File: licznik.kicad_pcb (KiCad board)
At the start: 2 copper layers, 71.1 x 43.2 mm, 23 parts, among them J1 Display, J2 Micro_SD_Card_Det, J3 Serial CS1, J4 Serial CS2, SW1 Wheel, SW2 Crank, SW3 Backlight, SW4 Right, SW5 Select, SW6 Left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

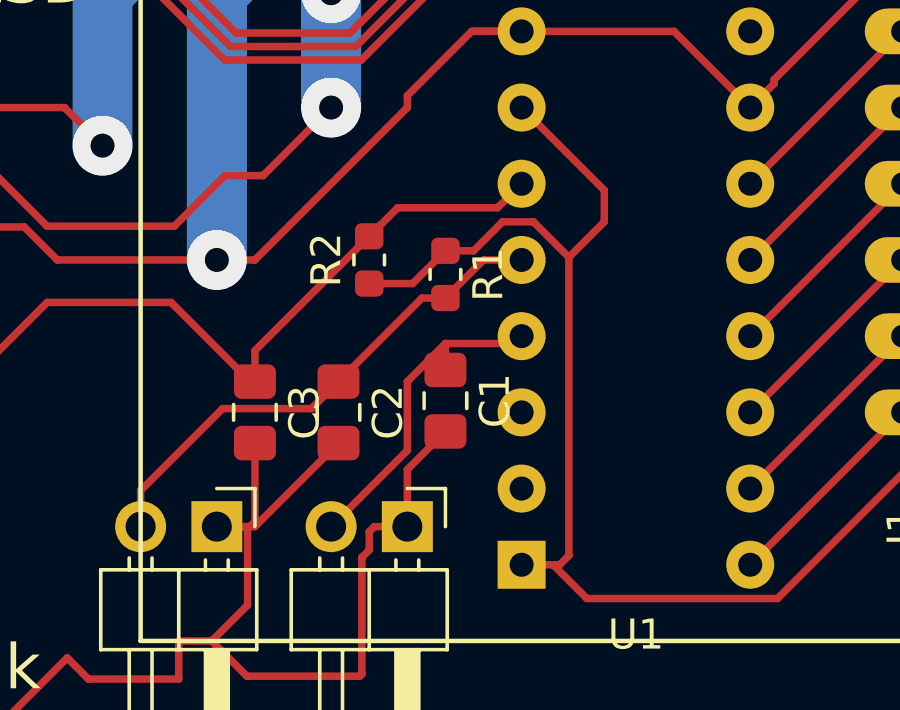
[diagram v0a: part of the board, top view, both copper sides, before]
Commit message: Add crank pull up resistor
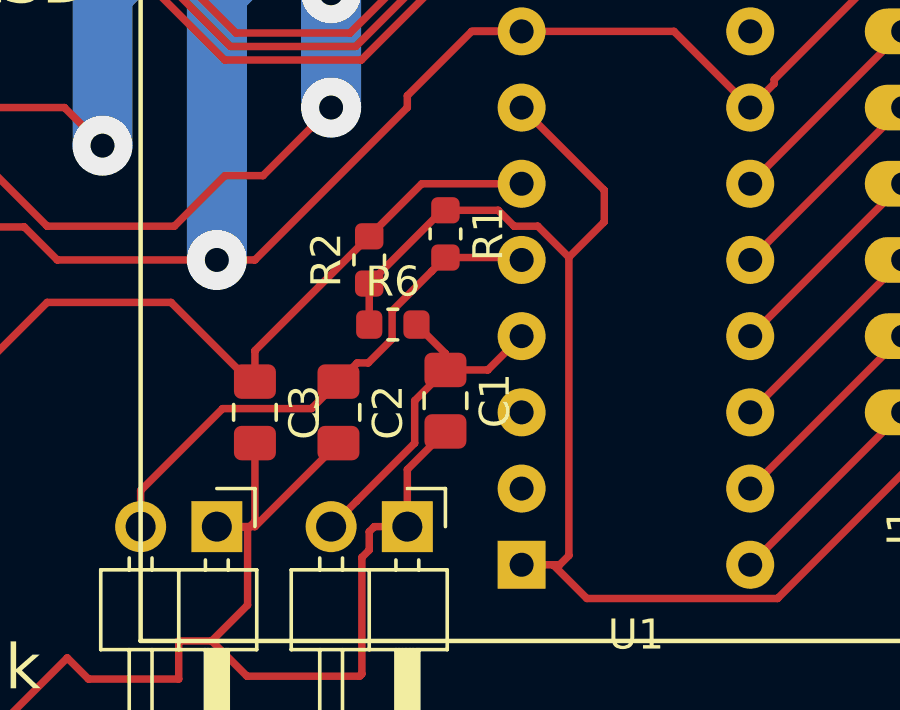
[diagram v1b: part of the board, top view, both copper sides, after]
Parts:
- added R6: 1K, Resistor_SMD:R_0603_1608Metric, F.Cu at (71.9, 184.2)
- moved R1 1.35 mm to (73.7, 181.1)
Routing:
- net +BATT: track 137.6 -> 139.3 mm
- net Net-(C2-Pad1): track 17.1 -> 17.7 mm
- net Net-(C1-Pad1): track 11.2 -> 11.7 mm
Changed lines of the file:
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@@
     (thickness 1.6)
     (drawings 14)
-    (tracks 267)
+    (tracks 273)
     (zones 0)
-    (modules 23)
+    (modules 24)
     (nets 26)
   )
@@
     (uvia_dia 0.3)
     (uvia_drill 0.1)
+  )
+  (module Resistor_SMD:R_0603_1608Metric (layer F.Cu)
+    (at 71.9075 184.15)
+    (descr "Resistor SMD 0603 (1608 Metric), square (rectangular) end terminal, IPC_7351 nominal, (Body size source: http://www.tortai-tech.com/upload/download/2011102023233369053.pdf), generated with kicad-footprint-generator")
+    (tags resistor)
+    (attr smd)
+    (fp_text reference R6 (at 0 -1.43) (layer F.SilkS)
+      (effects (font (size 1 1) (thickness 0.15)))
+    )
+    (fp_text value 1K (at 0 1.43) (layer F.Fab)
+      (effects (font (size 1 1) (thickness 0.15)))
+    )
+    (fp_line (start -0.8 0.4) (end -0.8 -0.4) (layer F.Fab) (width 0.1))
+    (fp_line (start -0.8 -0.4) (end 0.8 -0.4) (layer F.Fab) (width 0.1))
+    (fp_line (start 0.8 -0.4) (end 0.8 0.4) (layer F.Fab) (width 0.1))
+    (fp_line (start 0.8 0.4) (end -0.8 0.4) (layer F.Fab) (width 0.1))
+    (fp_line (start -0.162779 -0.51) (end 0.162779 -0.51) (layer F.SilkS) (width 0.12))
+    (fp_line (start -0.162779 0.51) (end 0.162779 0.51) (layer F.SilkS) (width 0.12))
+    (fp_line (start -1.48 0.73) (end -1.48 -0.73) (layer F.CrtYd) (width 0.05))
+    (fp_line (start -1.48 -0.73) (end 1.48 -0.73) (layer F.CrtYd) (width 0.05))
+    (fp_line (start 1.48 -0.73) (end 1.48 0.73) (layer F.CrtYd) (width 0.05))
+    (fp_line (start 1.48 0.73) (end -1.48 0.73) (layer F.CrtYd) (width 0.05))
+    (fp_text user %R (at 0 0) (layer F.Fab)
+      (effects (font (size 0.4 0.4) (thickness 0.06)))
+    )
+    (pad 1 smd roundrect (at -0.7875 0) (size 0.875 0.95) (layers F.Cu F.Paste F.Mask) (roundrect_rratio 0.25)
+      (net 22 +BATT))
+    (pad 2 smd roundrect (at 0.7875 0) (size 0.875 0.95) (layers F.Cu F.Paste F.Mask) (roundrect_rratio 0.25)
+      (net 1 "Net-(C1-Pad1)"))
+    (model ${KISYS3DMOD}/Resistor_SMD.3dshapes/R_0603_1608Metric.wrl
+      (at (xyz 0 0 0))
+      (scale (xyz 1 1 1))
+      (rotate (xyz 0 0 0))
+    )
   )
   (module Licznik:SD_pins (layer F.Cu)
@@
   )
   (module Resistor_SMD:R_0603_1608Metric (layer F.Cu)
-    (at 73.66 182.478122 270)
+    (at 73.66 181.1275 270)
     (descr "Resistor SMD 0603 (1608 Metric), square (rectangular) end terminal, IPC_7351 nominal, (Body size source: http://www.tortai-tech.com/upload/download/2011102023233369053.pdf), generated with kicad-footprint-generator")
     (tags resistor)
@@
   (gr_line (start 25.4 199.775622) (end 25.4 156.595622) (angle 90) (layer Edge.Cuts) (width 0.1))
   (gr_line (start 25.4 199.775622) (end 96.52 199.775622) (angle 90) (layer Edge.Cuts) (width 0.1))
-  (segment (start 75.955 184.780622) (end 76.2 184.535622) (width 0.25) (layer F.Cu) (net 1) (status 30))
-  (segment (start 73.66 184.780622) (end 75.955 184.780622) (width 0.25) (layer F.Cu) (net 1) (status 20))
-  (segment (start 73.66 185.662032) (end 73.66 184.780622) (width 0.25) (layer F.Cu) (net 1) (status 10))
-  (segment (start 73.66 184.780622) (end 72.39 186.050622) (width 0.25) (layer F.Cu) (net 1))
-  (segment (start 72.39 188.345622) (end 69.85 190.885622) (width 0.25) (layer F.Cu) (net 1) (status 20))
-  (segment (start 72.39 186.050622) (end 72.39 188.345622) (width 0.25) (layer F.Cu) (net 1))
+  (segment (start 75.07359 185.662032) (end 76.2 184.535622) (width 0.25) (layer F.Cu) (net 1))
+  (segment (start 73.66 185.662032) (end 75.07359 185.662032) (width 0.25) (layer F.Cu) (net 1))
+  (segment (start 70.699999 190.035623) (end 69.85 190.885622) (width 0.25) (layer F.Cu) (net 1))
+  (segment (start 72.63499 188.100632) (end 70.699999 190.035623) (width 0.25) (layer F.Cu) (net 1))
+  (segment (start 72.63499 186.687042) (end 72.63499 188.100632) (width 0.25) (layer F.Cu) (net 1))
+  (segment (start 73.66 185.662032) (end 72.63499 186.687042) (width 0.25) (layer F.Cu) (net 1))
+  (segment (start 73.66 185.115) (end 72.695 184.15) (width 0.25) (layer F.Cu) (net 1))
+  (segment (start 73.66 185.662032) (end 73.66 185.115) (width 0.25) (layer F.Cu) (net 1))
   (segment (start 83.82 179.455622) (end 88.9 174.375622) (width 0.25) (layer F.Cu) (net 5) (status 30))
   (segment (start 83.82 181.995622) (end 88.9 176.915622) (width 0.25) (layer F.Cu) (net 6) (status 30))
@@
   (segment (start 64.51499 183.410612) (end 67.31 186.205622) (width 0.25) (layer F.Cu) (net 14) (status 20))
   (segment (start 67.31 185.018122) (end 67.31 186.050622) (width 0.25) (layer F.Cu) (net 14) (status 20))
-  (segment (start 75.400001 180.255621) (end 72.072501 180.255621) (width 0.25) (layer F.Cu) (net 14) (status 10))
-  (segment (start 72.072501 180.255621) (end 71.12 181.208122) (width 0.25) (layer F.Cu) (net 14) (status 20))
-  (segment (start 76.2 179.455622) (end 75.400001 180.255621) (width 0.25) (layer F.Cu) (net 14) (status 30))
   (segment (start 71.12 181.208122) (end 67.31 185.018122) (width 0.25) (layer F.Cu) (net 14) (status 10))
   (segment (start 54.178976 189.615622) (end 60.383986 183.410612) (width 0.25) (layer F.Cu) (net 14))
   (segment (start 40.06 196.115622) (end 40.06 189.615622) (width 0.25) (layer F.Cu) (net 14) (status 30))
   (segment (start 40.06 189.615622) (end 54.178976 189.615622) (width 0.25) (layer F.Cu) (net 14) (status 10))
+  (segment (start 72.8725 179.455622) (end 76.2 179.455622) (width 0.25) (layer F.Cu) (net 14))
+  (segment (start 71.12 181.208122) (end 72.8725 179.455622) (width 0.25) (layer F.Cu) (net 14))
   (segment (start 63.5 189.683541) (end 63.5 190.885622) (width 0.25) (layer F.Cu) (net 15) (status 20))
   (segment (start 66.232909 186.950632) (end 63.5 189.683541) (width 0.25) (layer F.Cu) (net 15))
   (segment (start 69.19499 186.950632) (end 66.232909 186.950632) (width 0.25) (layer F.Cu) (net 15))
   (segment (start 70.095 186.050622) (end 69.19499 186.950632) (width 0.25) (layer F.Cu) (net 15) (status 10))
-  (segment (start 76.2 181.995622) (end 74.93 181.995622) (width 0.25) (layer F.Cu) (net 15) (status 10))
-  (segment (start 74.93 181.995622) (end 73.66 183.265622) (width 0.25) (layer F.Cu) (net 15) (status 20))
-  (segment (start 73.66 183.265622) (end 72.88 183.265622) (width 0.25) (layer F.Cu) (net 15) (status 10))
-  (segment (start 72.88 183.265622) (end 70.095 186.050622) (width 0.25) (layer F.Cu) (net 15) (status 20))
+  (segment (start 73.198388 182.376612) (end 73.66 181.915) (width 0.25) (layer F.Cu) (net 15))
+  (segment (start 71.88251 183.69249) (end 73.198388 182.376612) (width 0.25) (layer F.Cu) (net 15))
+  (segment (start 71.086744 185.42725) (end 71.88251 184.631484) (width 0.25) (layer F.Cu) (net 15))
+  (segment (start 71.88251 184.631484) (end 71.88251 183.69249) (width 0.25) (layer F.Cu) (net 15))
+  (segment (start 70.718372 185.42725) (end 71.086744 185.42725) (width 0.25) (layer F.Cu) (net 15))
+  (segment (start 70.095 186.050622) (end 70.718372 185.42725) (width 0.25) (layer F.Cu) (net 15))
+  (segment (start 76.119378 181.915) (end 76.2 181.995622) (width 0.25) (layer F.Cu) (net 15))
+  (segment (start 73.66 181.915) (end 76.119378 181.915) (width 0.25) (layer F.Cu) (net 15))
   (segment (start 66.889999 165.905623) (end 66.04 166.755622) (width 0.25) (layer F.Cu) (net 16) (status 30))
   (segment (start 70.33001 162.465612) (end 66.889999 165.905623) (width 0.25) (layer F.Cu) (net 16) (status 20))
@@
   (segment (start 73.66 165.968122) (end 74.1425 165.485622) (width 0.25) (layer F.Cu) (net 22))
   (segment (start 73.66 166.755622) (end 73.66 165.968122) (width 0.25) (layer F.Cu) (net 22) (status 10))
-  (segment (start 76.595002 180.725622) (end 77.77501 181.90563) (width 0.25) (layer F.Cu) (net 22))
-  (segment (start 75.56359 180.725622) (end 76.595002 180.725622) (width 0.25) (layer F.Cu) (net 22))
-  (segment (start 74.59859 181.690622) (end 75.56359 180.725622) (width 0.25) (layer F.Cu) (net 22))
-  (segment (start 73.66 181.690622) (end 74.59859 181.690622) (width 0.25) (layer F.Cu) (net 22) (status 10))
-  (segment (start 73.66 181.690622) (end 72.5675 182.783122) (width 0.25) (layer F.Cu) (net 22) (status 10))
-  (segment (start 72.5675 182.783122) (end 71.12 182.783122) (width 0.25) (layer F.Cu) (net 22) (status 20))
   (segment (start 81.759996 164.610624) (end 83.424998 162.945622) (width 0.25) (layer F.Cu) (net 22))
   (segment (start 77.47 164.610624) (end 81.759996 164.610624) (width 0.25) (layer F.Cu) (net 22))
@@
   (segment (start 76.2 176.915622) (end 78.955018 179.67064) (width 0.25) (layer F.Cu) (net 22) (status 10))
   (segment (start 77.77501 181.90563) (end 78.955018 180.725622) (width 0.25) (layer F.Cu) (net 22))
+  (segment (start 71.12 184.15) (end 71.12 182.783122) (width 0.25) (layer F.Cu) (net 22))
+  (segment (start 73.563122 180.34) (end 73.66 180.34) (width 0.25) (layer F.Cu) (net 22))
+  (segment (start 71.12 182.783122) (end 73.563122 180.34) (width 0.25) (layer F.Cu) (net 22))
+  (segment (start 76.740001 180.870621) (end 77.77501 181.90563) (width 0.25) (layer F.Cu) (net 22))
+  (segment (start 75.949997 180.870621) (end 76.740001 180.870621) (width 0.25) (layer F.Cu) (net 22))
+  (segment (start 75.419376 180.34) (end 75.949997 180.870621) (width 0.25) (layer F.Cu) (net 22))
+  (segment (start 73.66 180.34) (end 75.419376 180.34) (width 0.25) (layer F.Cu) (net 22))
   (segment (start 83.020001 158.335623) (end 83.82 159.135622) (width 0.25) (layer F.Cu) (net 23) (status 30))
   (segment (start 82.569991 157.885613) (end 83.020001 158.335623) (width 0.25) (layer F.Cu) (net 23) (status 20))

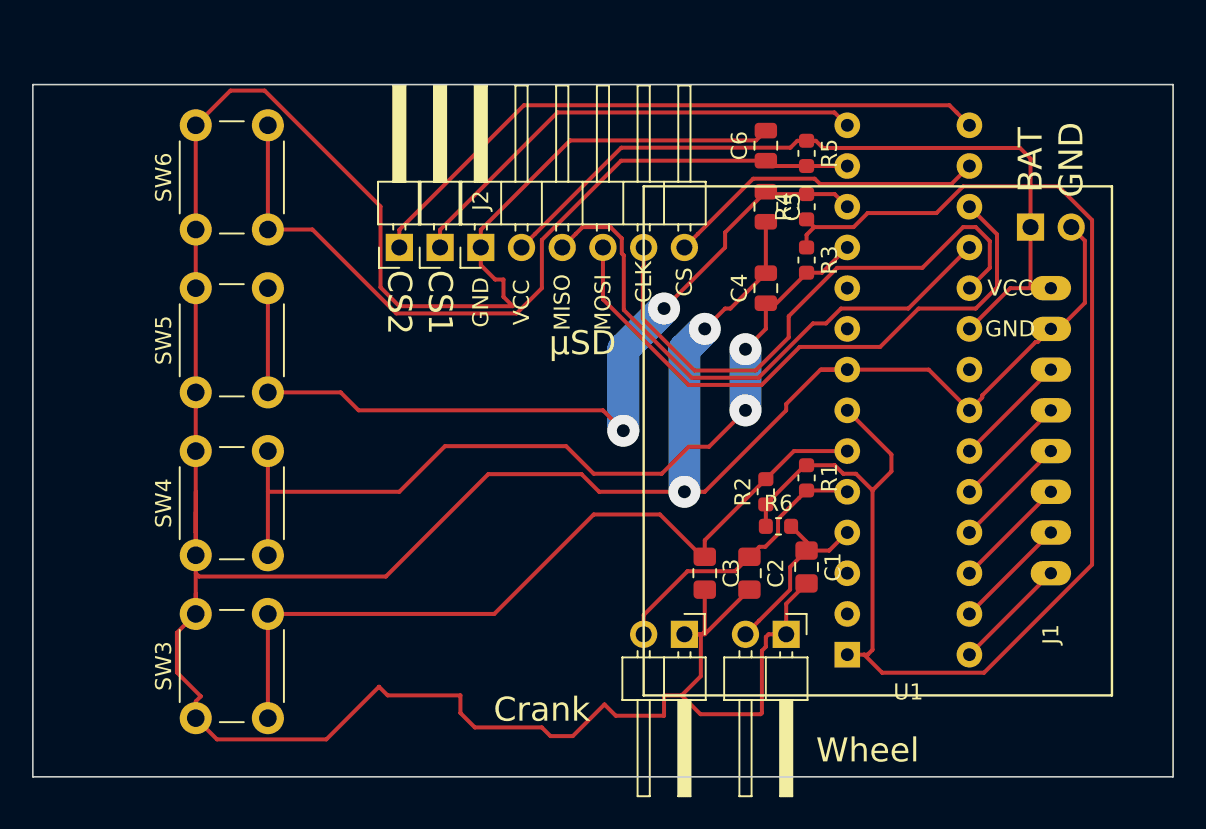
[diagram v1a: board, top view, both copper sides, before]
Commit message: Dimensions trim, reroute edy trace
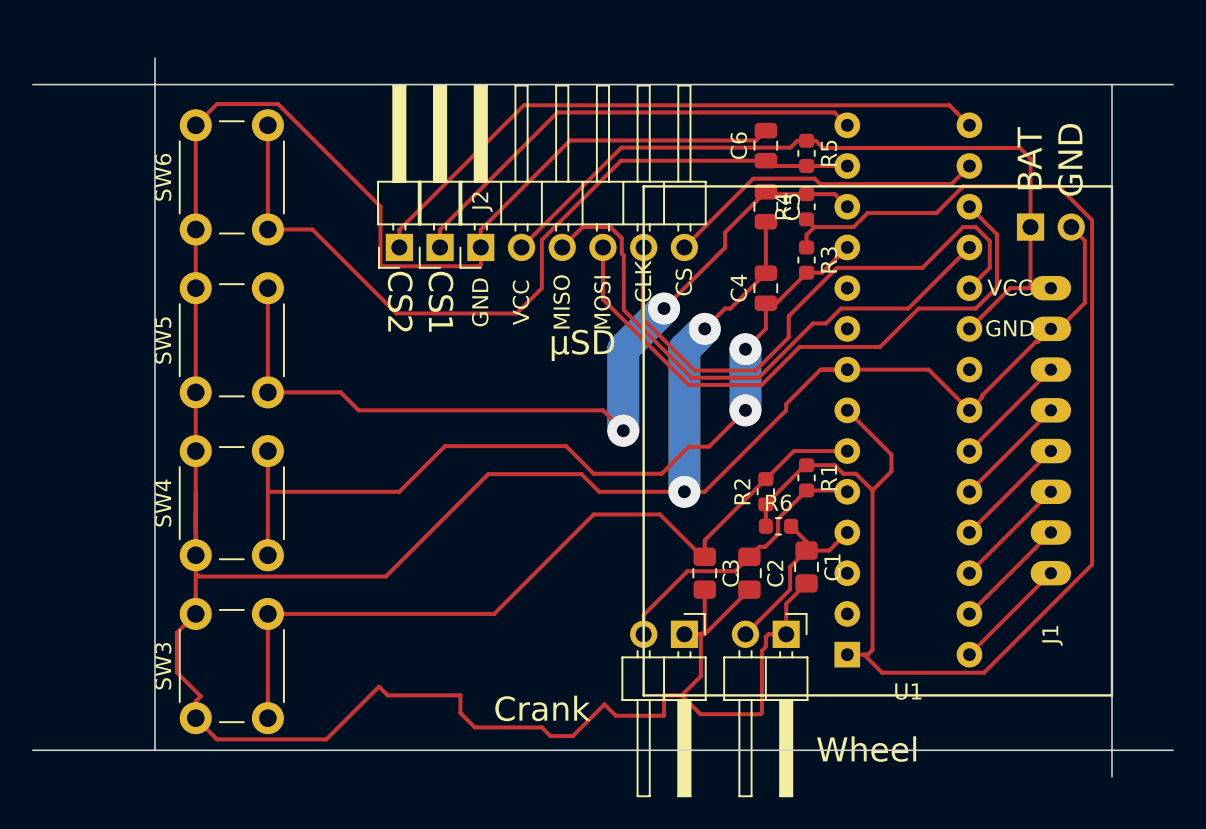
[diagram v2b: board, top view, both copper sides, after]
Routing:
- net GND: track 257.3 -> 249.1 mm
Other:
- board size 71.1 x 43.2 mm -> 71.1 x 44.8 mm
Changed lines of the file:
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@@
     (thickness 1.6)
     (drawings 14)
-    (tracks 273)
+    (tracks 270)
     (zones 0)
     (modules 24)
@@
     (effects (font (size 1.5 1.5) (thickness 0.3)))
   )
-  (gr_line (start 96.52 199.775622) (end 96.52 156.595622) (angle 90) (layer Edge.Cuts) (width 0.1))
+  (gr_line (start 92.71 199.775622) (end 92.71 156.595622) (angle 90) (layer Edge.Cuts) (width 0.1))
   (gr_line (start 25.4 156.595622) (end 96.52 156.595622) (angle 90) (layer Edge.Cuts) (width 0.1))
-  (gr_line (start 25.4 199.775622) (end 25.4 156.595622) (angle 90) (layer Edge.Cuts) (width 0.1))
-  (gr_line (start 25.4 199.775622) (end 96.52 199.775622) (angle 90) (layer Edge.Cuts) (width 0.1))
+  (gr_line (start 33.02 198.12) (end 33.02 154.94) (angle 90) (layer Edge.Cuts) (width 0.1))
+  (gr_line (start 25.4 198.12) (end 96.52 198.12) (angle 90) (layer Edge.Cuts) (width 0.1))
   (segment (start 75.07359 185.662032) (end 76.2 184.535622) (width 0.25) (layer F.Cu) (net 1))
   (segment (start 73.66 185.662032) (end 75.07359 185.662032) (width 0.25) (layer F.Cu) (net 1))
@@
   (segment (start 34.384999 193.265623) (end 34.384999 190.790623) (width 0.25) (layer F.Cu) (net 24))
   (segment (start 35.874997 194.755621) (end 34.384999 193.265623) (width 0.25) (layer F.Cu) (net 24))
-  (segment (start 54.239999 168.755621) (end 53.34 167.855622) (width 0.25) (layer F.Cu) (net 24))
-  (segment (start 54.754999 168.755621) (end 54.239999 168.755621) (width 0.25) (layer F.Cu) (net 24))
-  (segment (start 54.754999 169.835623) (end 54.754999 168.755621) (width 0.25) (layer F.Cu) (net 24))
-  (segment (start 53.34 167.855622) (end 53.34 166.755622) (width 0.25) (layer F.Cu) (net 24) (status 20))
-  (segment (start 55.339999 170.420623) (end 54.754999 169.835623) (width 0.25) (layer F.Cu) (net 24))
-  (segment (start 47.084999 169.245622) (end 48.26 170.420623) (width 0.25) (layer F.Cu) (net 24))
-  (segment (start 48.26 170.420623) (end 55.339999 170.420623) (width 0.25) (layer F.Cu) (net 24))
-  (segment (start 35.56 159.135622) (end 37.72499 156.970632) (width 0.25) (layer F.Cu) (net 24) (status 10))
-  (segment (start 39.856012 156.970632) (end 47.084999 164.199619) (width 0.25) (layer F.Cu) (net 24))
-  (segment (start 37.72499 156.970632) (end 39.856012 156.970632) (width 0.25) (layer F.Cu) (net 24))
-  (segment (start 47.084999 164.199619) (end 47.084999 169.245622) (width 0.25) (layer F.Cu) (net 24))
   (segment (start 35.56 165.635622) (end 35.56 169.295622) (width 0.25) (layer F.Cu) (net 24) (status 30))
   (segment (start 35.56 169.295622) (end 35.56 175.795622) (width 0.25) (layer F.Cu) (net 24) (status 30))
@@
   (segment (start 47.53 194.695622) (end 52.07 194.695622) (width 0.25) (layer F.Cu) (net 24))
   (segment (start 46.99 194.155622) (end 47.53 194.695622) (width 0.25) (layer F.Cu) (net 24))
+  (segment (start 47.084999 164.199619) (end 47.084999 167.865623) (width 0.25) (layer F.Cu) (net 24))
+  (segment (start 40.696001 157.810621) (end 47.084999 164.199619) (width 0.25) (layer F.Cu) (net 24))
+  (segment (start 36.885001 157.810621) (end 40.696001 157.810621) (width 0.25) (layer F.Cu) (net 24))
+  (segment (start 35.56 159.135622) (end 36.885001 157.810621) (width 0.25) (layer F.Cu) (net 24))
+  (segment (start 47.149999 167.930623) (end 47.084999 167.865623) (width 0.25) (layer F.Cu) (net 24))
+  (segment (start 53.264999 167.930623) (end 47.149999 167.930623) (width 0.25) (layer F.Cu) (net 24))
+  (segment (start 53.34 167.855622) (end 53.264999 167.930623) (width 0.25) (layer F.Cu) (net 24))
+  (segment (start 53.34 166.755622) (end 53.34 167.855622) (width 0.25) (layer F.Cu) (net 24))
   (segment (start 50.8 165.655622) (end 50.8 166.755622) (width 0.25) (layer F.Cu) (net 25) (status 20))
   (segment (start 58.119999 158.335623) (end 50.8 165.655622) (width 0.25) (layer F.Cu) (net 25))
